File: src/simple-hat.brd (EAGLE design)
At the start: 100 x 80 mm, 36 parts

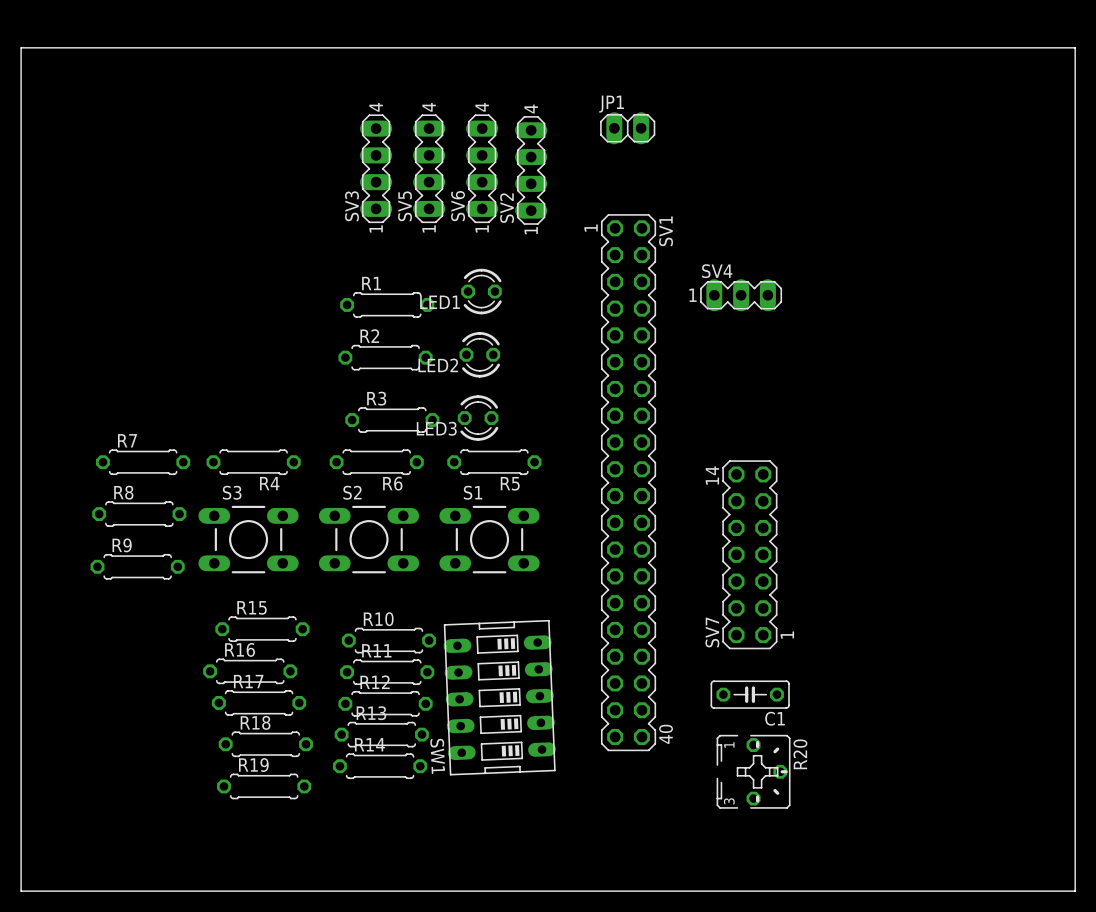
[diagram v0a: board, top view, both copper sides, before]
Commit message: Added routed borad data
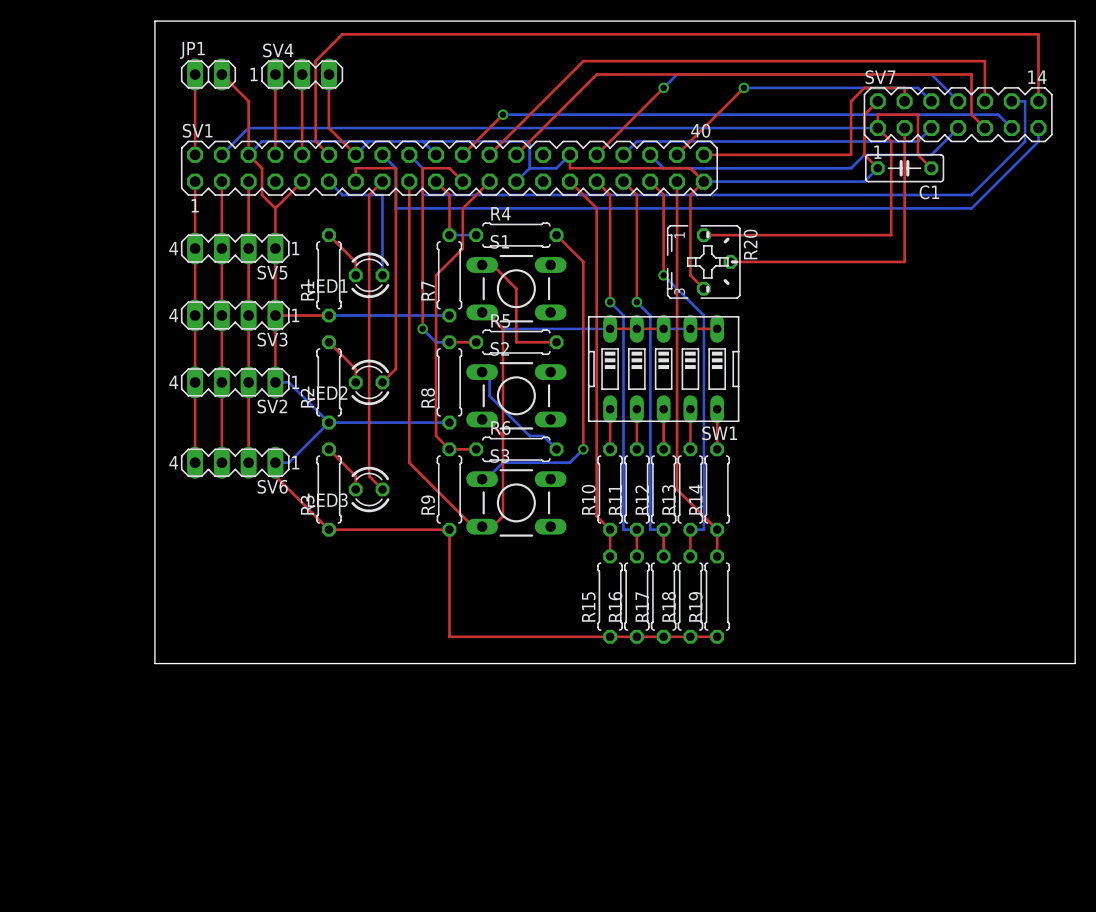
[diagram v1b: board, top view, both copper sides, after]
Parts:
- JP1: value (none) -> FAN
- LED1: value (none) -> USER1
- LED2: value (none) -> USER2
- LED3: value (none) -> USER3
- SV1: value (none) -> GPIO
- SV2: value (none) -> I2C_1
- SV3: value (none) -> I2C_2
- SV4: value (none) -> UART
- SV5: value (none) -> I2C_3
- SV6: value (none) -> I2C_4
- SV7: value (none) -> LCD
- SW1: value (none) -> USER4
- moved C1 52.0 mm to (83.8, 68.6)
- moved R20 48.6 mm to (64.8, 59.7)
- moved SV4 46.6 mm to (26.7, 77.5)
- moved R19 46.6 mm to (66.0, 27.9), turned to 90 degrees
- moved SV7 46.2 mm to (88.9, 73.7), turned to 0 degrees
- moved R18 42.6 mm to (63.5, 27.9), turned to 90 degrees
- moved R14 41.4 mm to (66.0, 38.1), turned to 90 degrees
- moved JP1 40.1 mm to (17.8, 77.5)
- moved R17 39.7 mm to (61.0, 27.9), turned to 90 degrees
- moved R13 37.4 mm to (63.5, 38.1), turned to 90 degrees
- moved R16 37.4 mm to (58.4, 27.9), turned to 90 degrees
- moved SV6 36.4 mm to (20.3, 40.6), turned to 180 degrees
- moved SW1 34.8 mm to (61.0, 49.5), turned to 180 degrees
- moved SV2 34.5 mm to (20.3, 48.3), turned to 180 degrees
- moved SV1 34.3 mm to (40.6, 68.6), turned to 0 degrees
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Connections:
- removed net GND06: JP1.2, SV1.6, SV4.3
- removed net GND09: R1.1, R2.1, R3.1, SV1.9, SV2.1, SV3.1, SV5.1, SV6.1
- removed net GND_25: R15.1, R16.1, R17.1, R18.1, R19.1, R7.1, R8.1, R9.1, SV1.25
- new net GND: C1.2, JP1.2, R1.1, R15.1, R16.1, R17.1, R18.1, R19.1, R2.1, R20.E, R3.1, R7.1, R8.1, R9.1, SV1.14, SV1.20, SV1.25, SV1.30, SV1.39, SV1.6, SV1.9, SV2.1, SV3.1, SV4.3, SV5.1, SV6.1, SV7.2
- net GND34: no longer C1.2, R20.E, SV7.2
- net I2C_SCL: now also SV1.5
- net RXD0: now also SV4.2
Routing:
- net GND: track 0.00 -> 229.9 mm
- net +5V_04: track 0.00 -> 102.4 mm
- net DB7: track 0.00 -> 85.4 mm
- net +3.3V_17: track 0.00 -> 84.6 mm
- net DB6: track 0.00 -> 70.5 mm
- net DB5: track 0.00 -> 68.7 mm
- net DB3: track 0.00 -> 54.5 mm
- net DB4: track 0.00 -> 54.2 mm, vias 0 -> 1
- net DB2: track 0.00 -> 51.9 mm
- net GPIO19: track 0.00 -> 38.9 mm, vias 0 -> 1
- net DB1: track 0.00 -> 38.5 mm, vias 0 -> 1
- net GPIO6: track 0.00 -> 37.9 mm, vias 0 -> 1
- net GPIO13: track 0.00 -> 37.9 mm, vias 0 -> 1
- net GPIO26: track 0.00 -> 37.1 mm
- net GPIO5: track 0.00 -> 37.1 mm
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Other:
- board size 100 x 80 mm -> 87.3 x 61 mm
